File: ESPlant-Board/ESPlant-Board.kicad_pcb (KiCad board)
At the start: 4 copper layers, 24 x 46 mm, 49 parts, among them J1 Conn_01x05, U1 USB-C, U13 ESP32-C6-MINI-1-N4, U3 AHT20-F, U4 Tactile-Switch, U5 3.3V-Regulator, U6 Light sensor, U7 Tactile-Switch, U8 Slide-Switch, U9 Battery-Spring

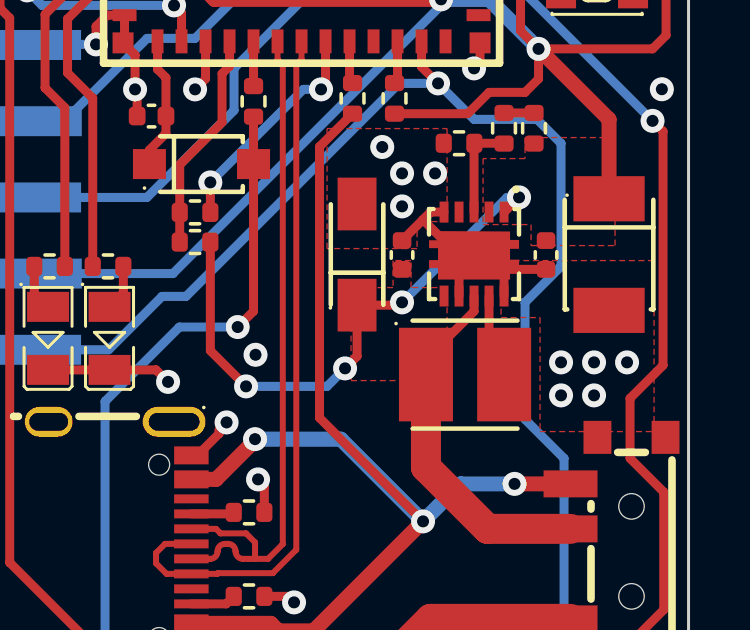
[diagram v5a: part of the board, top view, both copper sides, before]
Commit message: Board: Enable Power saving mode
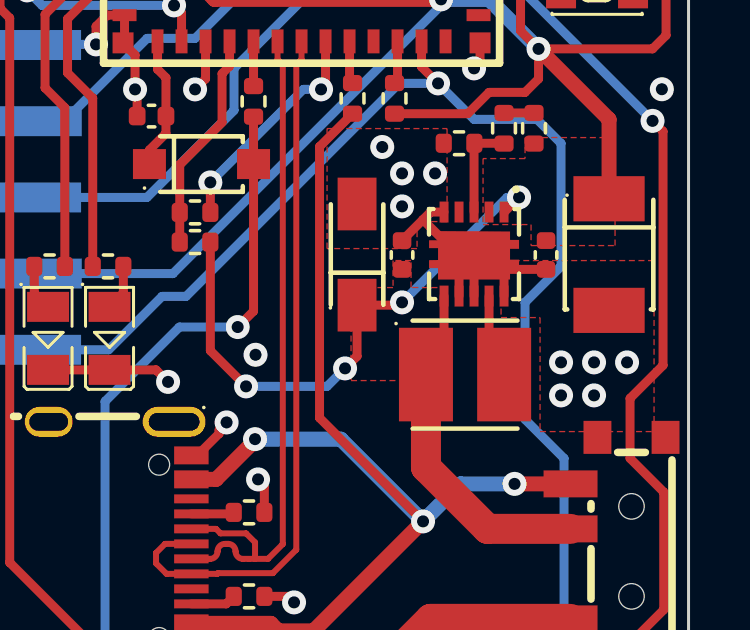
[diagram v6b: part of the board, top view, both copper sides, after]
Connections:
- U5 pad 8: PWR_VIN -> GND
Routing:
- net GND: track 218.5 -> 219.9 mm
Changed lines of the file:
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@@
       (net 2 "GND") (pinfunction "LBI") (pintype "passive"))
     (pad "8" smd rect (at 0 -1.400051) (size 0.3 0.7) (layers "F.Cu" "F.Paste" "F.Mask")
-      (net 29 "PWR_VIN") (pinfunction "PS") (pintype "input"))
+      (net 2 "GND") (pinfunction "PS") (pintype "input"))
     (pad "9" smd rect (at -0.499873 -1.400051 180) (size 0.3 0.7) (layers "F.Cu" "F.Paste" "F.Mask")
       (net 35 "PWR_SW") (pinfunction "SW") (pintype "input"))
@@
   (segment (start 167.374866 135.249727) (end 167.374866 133.44988) (width 0.3) (layer "F.Cu") (net 2))
   (segment (start 171.549872 128.799892) (end 172.349974 129.599994) (width 0.3) (layer "F.Cu") (net 2))
+  (segment (start 174.899998 146.889711) (end 174.899998 145.534872) (width 0.3) (layer "F.Cu") (net 2))
   (segment (start 173.899998 144.089609) (end 173.450383 144.089609) (width 0.3) (layer "F.Cu") (net 2))
   (segment (start 164.299936 128.549956) (end 164.349974 128.599994) (width 0.3) (layer "F.Cu") (net 2))
@@
   (segment (start 165.077946 147.922046) (end 162.599998 150.399994) (width 0.3) (layer "B.Cu") (net 28))
   (segment (start 162.599998 150.399994) (end 162.599998 165.099994) (width 0.3) (layer "B.Cu") (net 28))
-  (segment (start 174.899998 146.889711) (end 174.899998 147.399994) (width 0.3) (layer "F.Cu") (net 29))
+  (segment (start 173.899998 148.90328) (end 173.296975 149.506303) (width 0.3) (layer "F.Cu") (net 29))
   (segment (start 175.350062 154.650058) (end 173.296975 152.596971) (width 1) (layer "F.Cu") (net 29))
   (segment (start 178.116559 154.650058) (end 175.350062 154.650058) (width 1) (layer "F.Cu") (net 29))
+  (segment (start 173.899998 146.889711) (end 173.899998 148.90328) (width 0.3) (layer "F.Cu") (net 29))
   (segment (start 170.999998 147.192612) (end 172.40738 147.192612) (width 0.3) (layer "F.Cu") (net 29))
-  (segment (start 174.899998 147.399994) (end 173.296975 149.003017) (width 0.3) (layer "F.Cu") (net 29))
   (segment (start 166.109998 148.709994) (end 166.109998 145.089994) (width 0.3) (layer "F.Cu") (net 29))
   (segment (start 167.299998 149.899994) (end 166.109998 148.709994) (width 0.3) (layer "F.Cu") (net 29))

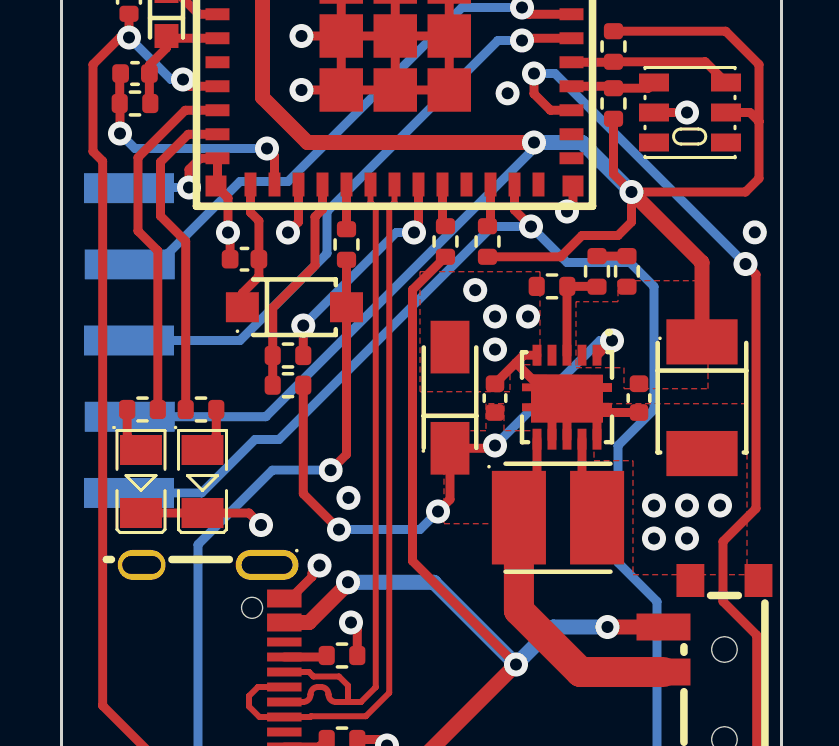
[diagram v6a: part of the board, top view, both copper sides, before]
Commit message: Panel: Add voltage divider for checking usb connection
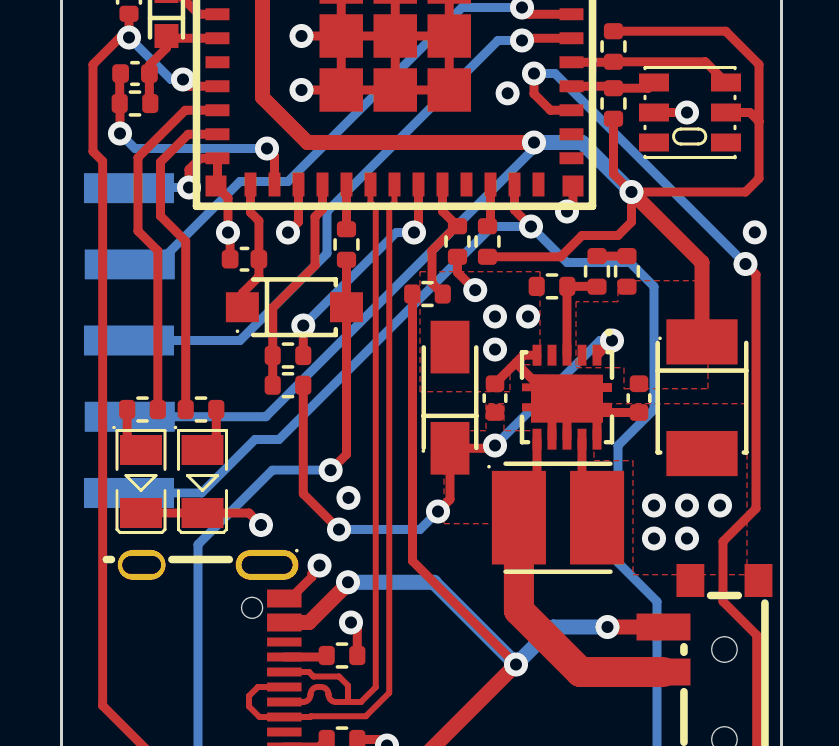
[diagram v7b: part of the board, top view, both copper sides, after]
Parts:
- added R17: 20k, Resistor_SMD:R_0402_1005Metric, F.Cu at (171.2, 140.3)
- moved R7 1.85 mm to (170.2, 142.0), turned to 0 degrees
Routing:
- net Net-(U13-IO15): track 1.43 -> 4.38 mm
- net PWR_USB_VIN: track 39.7 -> 38.0 mm
- net GND: track 219.9 -> 221.2 mm
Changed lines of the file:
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@@
   )
   (footprint "Resistor_SMD:R_0402_1005Metric" (layer "F.Cu")
-    (at 170.849999 140.299994 90)
+    (at 170.249999 142.049997)
     (descr "Resistor SMD 0402 (1005 Metric), square (rectangular) end terminal, IPC_7351 nominal, (Body size source: IPC-SM-782 page 72, https://www.pcb-3d.com/wordpress/wp-content/uploads/ipc-sm-782a_amendment_1_and_2.pdf), generated with kicad-footprint-generator")
     (tags "resistor")
@@
     (property "ki_keywords" "R res resistor")
     (attr smd)
-    (fp_text reference "R7" (at 0 1.05 90) (layer "F.SilkS") hide
-        (effects (font (size 1 1) (thickness 0.15)))
-    )
-    (fp_text value "10k" (at 0 1.17 90) (layer "F.Fab")
-        (effects (font (size 1 1) (thickness 0.15)))
-    )
-    (fp_text user "${REFERENCE}" (at 0 0 90) (layer "F.Fab")
+    (fp_text reference "R7" (at 0 1.05) (layer "F.SilkS") hide
+        (effects (font (size 1 1) (thickness 0.15)))
+    )
+    (fp_text value "10k" (at 0 1.17) (layer "F.Fab")
+        (effects (font (size 1 1) (thickness 0.15)))
+    )
+    (fp_text user "${REFERENCE}" (at 0 0) (layer "F.Fab")
         (effects (font (size 0.26 0.26) (thickness 0.04)))
     )
@@
     (fp_line (start 0.525 0.27) (end -0.525 0.27)
       (stroke (width 0.1) (type solid)) (layer "F.Fab"))
-    (pad "1" smd roundrect (at -0.51 0 90) (size 0.54 0.64) (layers "F.Cu" "F.Paste" "F.Mask") (roundrect_rratio 0.25)
+    (pad "1" smd roundrect (at -0.51 0) (size 0.54 0.64) (layers "F.Cu" "F.Paste" "F.Mask") (roundrect_rratio 0.25)
       (net 40 "PWR_USB_VIN") (pintype "passive"))
-    (pad "2" smd roundrect (at 0.51 0 90) (size 0.54 0.64) (layers "F.Cu" "F.Paste" "F.Mask") (roundrect_rratio 0.25)
+    (pad "2" smd roundrect (at 0.51 0) (size 0.54 0.64) (layers "F.Cu" "F.Paste" "F.Mask") (roundrect_rratio 0.25)
       (net 57 "Net-(U13-IO15)") (pintype "passive"))
     (model "${KICAD6_3DMODEL_DIR}/Resistor_SMD.3dshapes/R_0402_1005Metric.wrl"
@@
       (net 2 "GND") (pintype "passive"))
     (model "${KICAD6_3DMODEL_DIR}/Capacitor_SMD.3dshapes/C_0402_1005Metric.wrl"
+      (offset (xyz 0 0 0))
+      (scale (xyz 1 1 1))
+      (rotate (xyz 0 0 0))
+    )
+  )
+  (footprint "Resistor_SMD:R_0402_1005Metric" (layer "F.Cu")
+    (at 171.249999 140.299997 -90)
+    (descr "Resistor SMD 0402 (1005 Metric), square (rectangular) end terminal, IPC_7351 nominal, (Body size source: IPC-SM-782 page 72, https://www.pcb-3d.com/wordpress/wp-content/uploads/ipc-sm-782a_amendment_1_and_2.pdf), generated with kicad-footprint-generator")
+    (tags "resistor")
+    (property "LCSC" "C25765")
+    (property "MPN" "C25765")
+    (property "Sheetfile" "ESPlant-Board.kicad_sch")
+    (property "Sheetname" "")
+    (property "ki_description" "Resistor")
+    (property "ki_keywords" "R res resistor")
+    (attr smd)
+    (fp_text reference "R17" (at 0 -1.17 90) (layer "F.SilkS") hide
+        (effects (font (size 1 1) (thickness 0.15)))
+    )
+    (fp_text value "20k" (at 0 1.17 90) (layer "F.Fab")
+        (effects (font (size 1 1) (thickness 0.15)))
+    )
+    (fp_text user "${REFERENCE}" (at 0 0 90) (layer "F.Fab")
+        (effects (font (size 0.26 0.26) (thickness 0.04)))
+    )
+    (fp_line (start -0.153641 -0.38) (end 0.153641 -0.38)
+      (stroke (width 0.12) (type solid)) (layer "F.SilkS"))
+    (fp_line (start -0.153641 0.38) (end 0.153641 0.38)
+      (stroke (width 0.12) (type solid)) (layer "F.SilkS"))
+    (fp_line (start -0.93 -0.47) (end 0.93 -0.47)
+      (stroke (width 0.05) (type solid)) (layer "F.CrtYd"))
+    (fp_line (start -0.93 0.47) (end -0.93 -0.47)
+      (stroke (width 0.05) (type solid)) (layer "F.CrtYd"))
+    (fp_line (start 0.93 -0.47) (end 0.93 0.47)
+      (stroke (width 0.05) (type solid)) (layer "F.CrtYd"))
+    (fp_line (start 0.93 0.47) (end -0.93 0.47)
+      (stroke (width 0.05) (type solid)) (layer "F.CrtYd"))
+    (fp_line (start -0.525 -0.27) (end 0.525 -0.27)
+      (stroke (width 0.1) (type solid)) (layer "F.Fab"))
+    (fp_line (start -0.525 0.27) (end -0.525 -0.27)
+      (stroke (width 0.1) (type solid)) (layer "F.Fab"))
+    (fp_line (start 0.525 -0.27) (end 0.525 0.27)
+      (stroke (width 0.1) (type solid)) (layer "F.Fab"))
+    (fp_line (start 0.525 0.27) (end -0.525 0.27)
+      (stroke (width 0.1) (type solid)) (layer "F.Fab"))
+    (pad "1" smd roundrect (at -0.51 0 270) (size 0.54 0.64) (layers "F.Cu" "F.Paste" "F.Mask") (roundrect_rratio 0.25)
+      (net 57 "Net-(U13-IO15)") (pintype "passive"))
+    (pad "2" smd roundrect (at 0.51 0 270) (size 0.54 0.64) (layers "F.Cu" "F.Paste" "F.Mask") (roundrect_rratio 0.25)
+      (net 2 "GND") (pintype "passive"))
+    (model "${KICAD6_3DMODEL_DIR}/Resistor_SMD.3dshapes/R_0402_1005Metric.wrl"
       (offset (xyz 0 0 0))
       (scale (xyz 1 1 1))
@@
   (segment (start 177.299998 145.999994) (end 175.36512 145.999994) (width 0.3) (layer "F.Cu") (net 2))
   (segment (start 159.422413 162.907321) (end 159.615086 163.099994) (width 0.3) (layer "F.Cu") (net 2))
+  (segment (start 171.249999 141.330096) (end 171.840296 141.920393) (width 0.3) (layer "F.Cu") (net 2))
   (segment (start 172.349974 128.599994) (end 172.349974 129.599994) (width 0.3) (layer "F.Cu") (net 2))
   (segment (start 167.374866 131.649778) (end 169.174968 131.649778) (width 0.3) (layer "F.Cu") (net 2))
@@
   (segment (start 169.174968 133.44988) (end 170.974815 133.44988) (width 0.3) (layer "F.Cu") (net 2))
   (segment (start 167.374866 133.44988) (end 167.374866 131.649778) (width 0.3) (layer "F.Cu") (net 2))
+  (segment (start 171.249999 140.809997) (end 171.249999 141.330096) (width 0.3) (layer "F.Cu") (net 2))
   (segment (start 173.194997 144.344995) (end 172.499998 145.039994) (width 0.3) (layer "F.Cu") (net 2))
   (segment (start 174.399871 146.889711) (end 174.399871 146.034999) (width 0.3) (layer "F.Cu") (net 2))
@@
   (segment (start 172.349974 139.690019) (end 172.249999 139.789994) (width 0.3) (layer "F.Cu") (net 38))
   (segment (start 166.109998 143.099994) (end 166.109998 144.099994) (width 0.3) (layer "F.Cu") (net 39))
-  (segment (start 169.949923 138.399842) (end 169.949923 139.850069) (width 0.3) (layer "F.Cu") (net 39))
-  (segment (start 169.949923 139.850069) (end 169.799998 139.999994) (width 0.3) (layer "F.Cu") (net 39))
+  (segment (start 169.799998 139.999994) (end 169.949923 139.850069) (width 0.3) (layer "F.Cu") (net 39))
+  (segment (start 169.949923 139.850069) (end 169.949923 138.399842) (width 0.3) (layer "F.Cu") (net 39))
   (via (at 166.109998 143.099994) (size 0.8) (drill 0.4) (layers "F.Cu" "B.Cu") (net 39))
   (via (at 169.799998 139.999994) (size 0.8) (drill 0.4) (layers "F.Cu" "B.Cu") (net 39))
-  (segment (start 166.109998 143.099994) (end 169.209998 139.999994) (width 0.3) (layer "B.Cu") (net 39))
-  (segment (start 169.209998 139.999994) (end 169.799998 139.999994) (width 0.3) (layer "B.Cu") (net 39))
-  (segment (start 170.849999 140.809994) (end 169.749998 141.909995) (width 0.3) (layer "F.Cu") (net 40))
+  (segment (start 169.209998 139.999994) (end 166.109998 143.099994) (width 0.3) (layer "B.Cu") (net 39))
+  (segment (start 169.799998 139.999994) (end 169.209998 139.999994) (width 0.3) (layer "B.Cu") (net 39))
+  (segment (start 169.739999 142.049997) (end 169.749998 142.059996) (width 0.3) (layer "F.Cu") (net 40))
   (segment (start 169.549998 158.049994) (end 173.199998 154.399994) (width 0.5) (layer "F.Cu") (net 40))
+  (segment (start 176.250189 153.150185) (end 178.116559 153.150185) (width 0.5) (layer "F.Cu") (net 40))
   (segment (start 169.749998 150.949994) (end 173.199998 154.399994) (width 0.3) (layer "F.Cu") (net 40))
-  (segment (start 176.250189 153.150185) (end 178.116559 153.150185) (width 0.5) (layer "F.Cu") (net 40))
-  (segment (start 169.749998 141.909995) (end 169.749998 150.949994) (width 0.3) (layer "F.Cu") (net 40))
   (segment (start 167.599445 151.658513) (end 167.599445 151.700547) (width 0.5) (layer "F.Cu") (net 40))
+  (segment (start 169.749998 142.059996) (end 169.749998 150.949994) (width 0.3) (layer "F.Cu") (net 40))
   (segment (start 167.599445 151.700547) (end 166.300049 152.999943) (width 0.5) (layer "F.Cu") (net 40))
   (segment (start 168.124912 157.800045) (end 168.374861 158.049994) (width 0.5) (layer "F.Cu") (net 40))
@@
   (segment (start 173.449934 157.650058) (end 178.116559 157.650058) (width 1) (layer "F.Cu") (net 52))
   (segment (start 167.799995 172.299997) (end 170.199998 169.899994) (width 1) (layer "F.Cu") (net 52))
-  (segment (start 170.750025 138.399842) (end 170.750025 139.69002) (width 0.3) (layer "F.Cu") (net 57))
-  (segment (start 170.750025 139.69002) (end 170.849999 139.789994) (width 0.3) (layer "F.Cu") (net 57))
+  (segment (start 171.249999 139.789997) (end 170.750025 139.290023) (width 0.3) (layer "F.Cu") (net 57))
+  (segment (start 171.212077 139.789997) (end 171.249999 139.789997) (width 0.3) (layer "F.Cu") (net 57))
+  (segment (start 170.399999 140.602075) (end 171.212077 139.789997) (width 0.3) (layer "F.Cu") (net 57))
+  (segment (start 170.399999 141.689997) (end 170.399999 140.602075) (width 0.3) (layer "F.Cu") (net 57))
+  (segment (start 170.759999 142.049997) (end 170.399999 141.689997) (width 0.3) (layer "F.Cu") (net 57))
+  (segment (start 170.750025 139.290023) (end 170.750025 138.399842) (width 0.3) (layer "F.Cu") (net 57))
   (zone (net 29) (net_name "PWR_VIN") (layer "F.Cu") (hatch edge 0.5)
     (priority 2)

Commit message: Board: Change AHT20-F to AHT20
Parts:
- U3: value AHT20-F -> AHT20
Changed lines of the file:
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@@
     (descr "SENSOR-SMD-6_AHT20 footprint")
     (tags "SENSOR-SMD-6_AHT20 footprint C3012622")
-    (property "LCSC" "C3012622")
-    (property "MPN" "C3012622")
+    (property "LCSC" "C2757850")
+    (property "MPN" "C2757850")
     (property "Sheetfile" "ESPlant-Board.kicad_sch")
     (property "Sheetname" "")
@@
         (effects (font (size 1 1) (thickness 0.15)))
     )
-    (fp_text value "AHT20-F" (at 0 3.5) (layer "F.Fab")
+    (fp_text value "AHT20" (at 0 3.5) (layer "F.Fab")
         (effects (font (size 1 1) (thickness 0.15)))
     )
